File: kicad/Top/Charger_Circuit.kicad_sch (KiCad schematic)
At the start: 112 parts

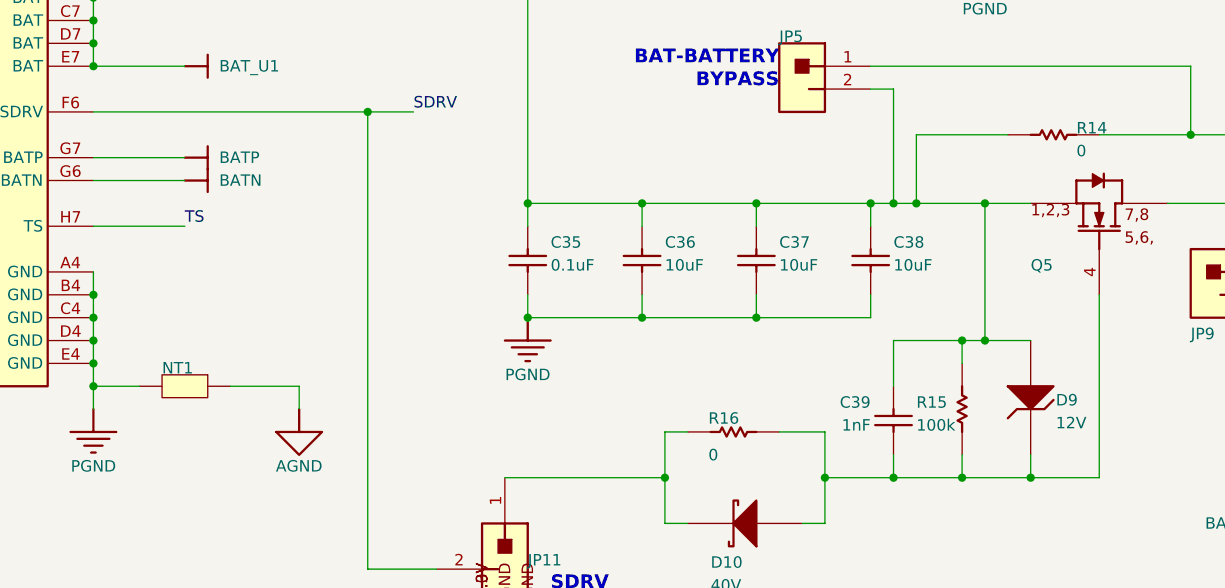
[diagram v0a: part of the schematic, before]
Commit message: Properly synced pcb to schematic
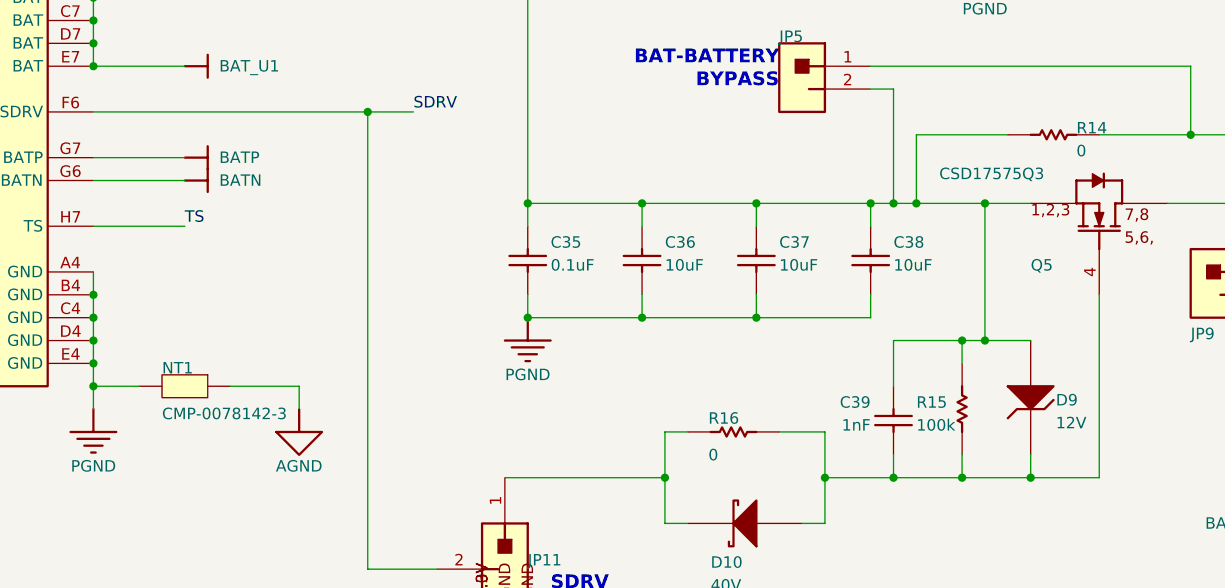
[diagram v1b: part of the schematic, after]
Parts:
- C10, C21, C22, C23, C27, C28, C29, C30, C31, C7, C8, C9: value ~ -> C2012X5R1E106K125AB; footprint 0805_HV -> AltiumImports:0805_HV
- C11, C14, C15, C24, C26: value ~ -> C1005X7R1H104K050BE; footprint 0402L -> AltiumImports:0402L
- C12, C6: value ~ -> GRM1885C1H222JA01D; footprint 0603 -> AltiumImports:0603
- C13, C3: value ~ -> GRM155R71E473KA88D; footprint 0402 -> AltiumImports:0402
- C16, C17: value ~ -> C0402C103J5RACTU; footprint 0402 -> AltiumImports:0402
- C34: value ~ -> GRM188R61C475KAAJD; footprint 0603L -> AltiumImports:0603L
- C35: value ~ -> GRM155R61E104KA87D; footprint 0402L -> AltiumImports:0402L
- C36, C37, C38: value ~ -> GRT188R61E106ME13D; footprint 0603L -> AltiumImports:0603L
- C39: value ~ -> GRM1555C1H102FA01D; footprint 0402 -> AltiumImports:0402
- C40, C41: value ~ -> GRM1555C1H102JA01D; footprint 0402L -> AltiumImports:0402L
- D10: value ~ -> CMP-0028378-3; footprint SOD-523 -> AltiumImports:SOD-523
- D3, D6, D7, D8: value ~ -> B130LAW-7-F; footprint SOD-123 -> AltiumImports:SOD-123
- D9: value ~ -> BZT52C12T-7; footprint SOD-523 -> AltiumImports:SOD-523
- J3: value ~ -> ED120/2DS; footprint On-Shore_ED120_2DS -> AltiumImports:On-Shore_ED120_2DS
- J5: value ~ -> ED120/4DS; footprint On-Shore_ED120_4DS -> AltiumImports:On-Shore_ED120_4DS
- JP1, JP11, JP2: value ~ -> PEC03SAAN; footprint CONN_PEC03SAAN -> AltiumImports:CONN_PEC03SAAN
- JP10, JP6: value ~ -> Header_2x1; footprint CONN_PEC02SAAN -> AltiumImports:CONN_PEC02SAAN
- JP12, JP13, JP9: value ~ -> CMP-0002337-1; footprint CONN_PEC02SAAN -> AltiumImports:CONN_PEC02SAAN
- JP3, JP4, JP5: value ~ -> HTSW-102-07-G-S; footprint Samtec_HTSW-102-07-G-S -> AltiumImports:Samtec_HTSW-102-07-G-S
- L1: value ~ -> MPIM252010F1R0M-LF; footprint MPIM252010F -> AltiumImports:MPIM252010F
- L2: value ~ -> SPM6530T-2R2M; footprint SPM6530 -> AltiumImports:SPM6530
- NT1: value ~ -> CMP-0078142-3; footprint Net-Tie_20milWide_60milLong -> AltiumImports:Net-Tie_20milWide_60milLong
- Q5: value ~ -> CSD17575Q3; footprint DQG0008A -> AltiumImports:DQG0008A
- R10, R8: value ~ -> CRCW06032R00JNEA; footprint 0603 -> AltiumImports:0603
- R12, R13: value ~ -> WSL2010R0100FEA18; footprint 2010 -> AltiumImports:2010
- R14: value ~ -> 5106; footprint 5106 -> AltiumImports:5106
- R15: value ~ -> RC0402FR-07100KL; footprint 0402 -> AltiumImports:0402
- R16: value ~ -> CMP-0025697-4; footprint 0603L -> AltiumImports:0603L
- R17, R18: value ~ -> RC0603FR-07100RL; footprint 0603 -> AltiumImports:0603
- R20, R44, R45: value ~ -> CRCW040210K0FKED; footprint 0402 -> AltiumImports:0402
- TP10, TP11, TP12, TP15, TP16, TP17, TP18, TP19, TP20, TP28, TP29, TP3, TP30, TP31, TP32, TP33, TP34, TP35, TP36, TP37, TP38, TP39, TP4, TP40, TP41, TP42, TP43, TP44, TP5, TP6, TP9: value ~ -> CMP-0055139-1; footprint Keystone5002 -> AltiumImports:Keystone5002
- TP21, TP22, TP23, TP24: value ~ -> CMP-0055137-1; footprint Keystone5000 -> AltiumImports:Keystone5000
- TP25, TP26: value ~ -> CMP-0055140-1; footprint Keystone5003 -> AltiumImports:Keystone5003
- TP27: value ~ -> CMP-0055141-1; footprint Keystone5004 -> AltiumImports:Keystone5004
- TP45, TP46, TP47, TP48, TP49, TP50, TP51: value ~ -> CMP-0055153-1; footprint Testpoint_Keystone_Compact -> AltiumImports:Testpoint_Keystone_Compact
- U1: value ~ -> BQ25790YBG; footprint PREYBG0056 -> AltiumImports:PREYBG0056
